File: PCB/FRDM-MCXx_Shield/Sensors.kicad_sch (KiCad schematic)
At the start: 9 parts, among them J7 Conn_01x06_Socket, U2 FXLS8974CF

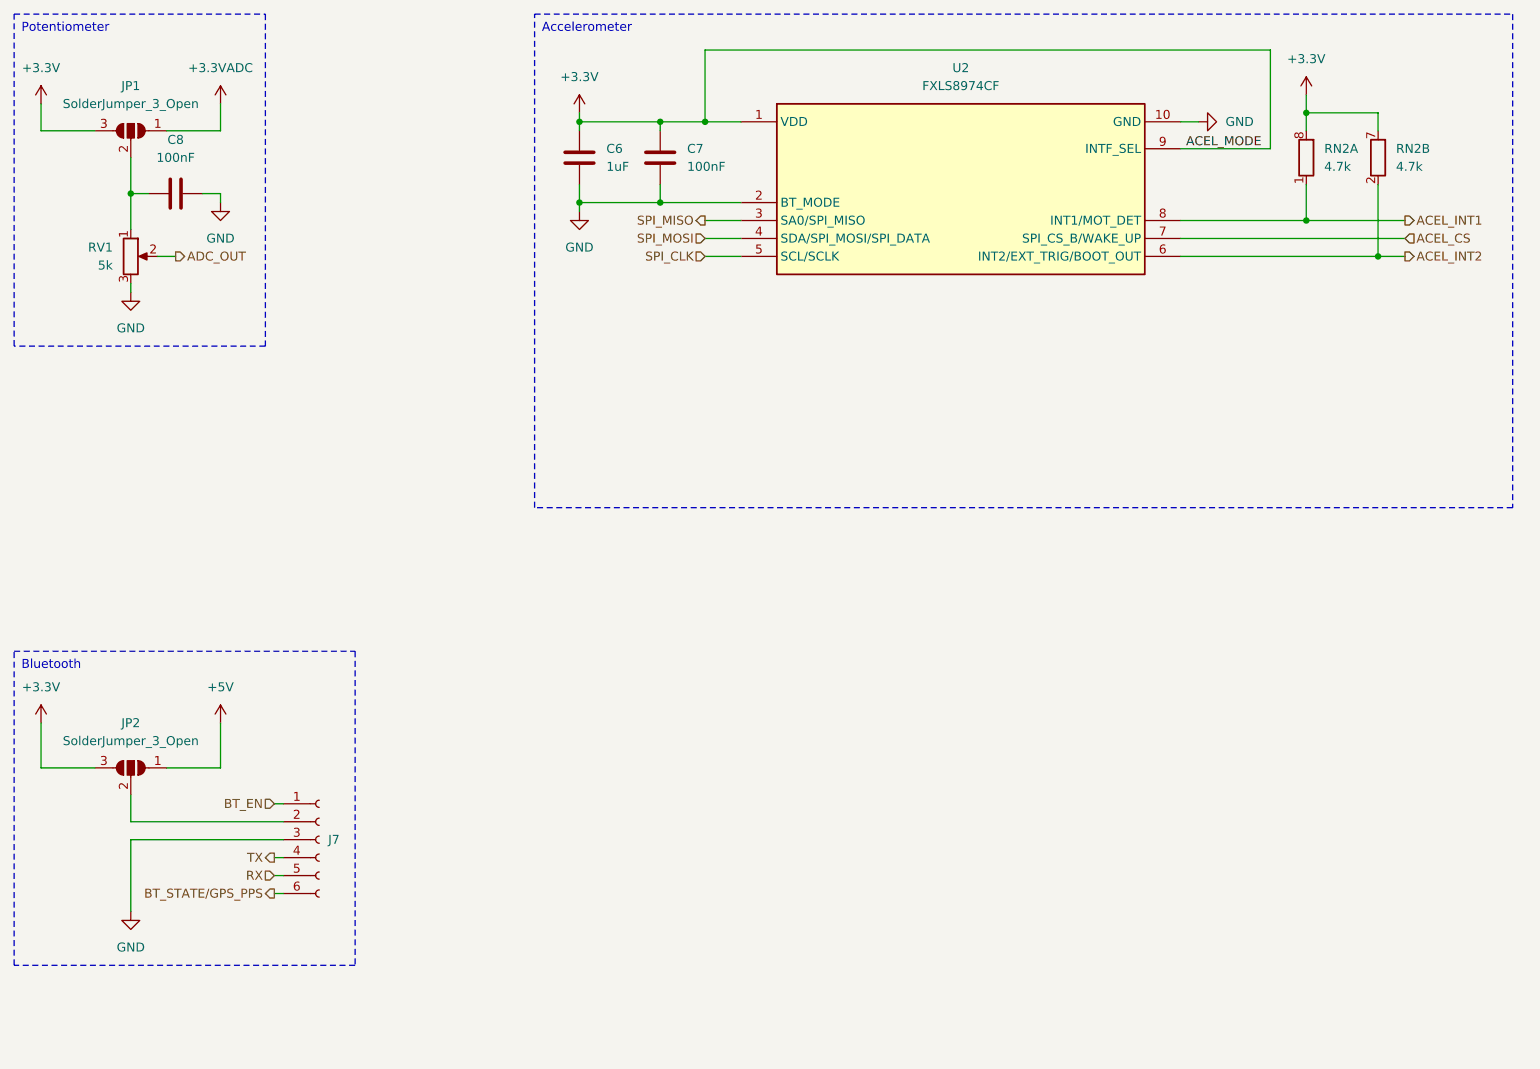
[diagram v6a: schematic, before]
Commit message: Update
Schematic: Fixed pinout, removed 5-9vin and a bunch of other stuff. Changed button/encoder debouncing.

PCB: Fixed pinout, layout and labeling. Added extra resisitors and capacitors.
Added diode direction markers.
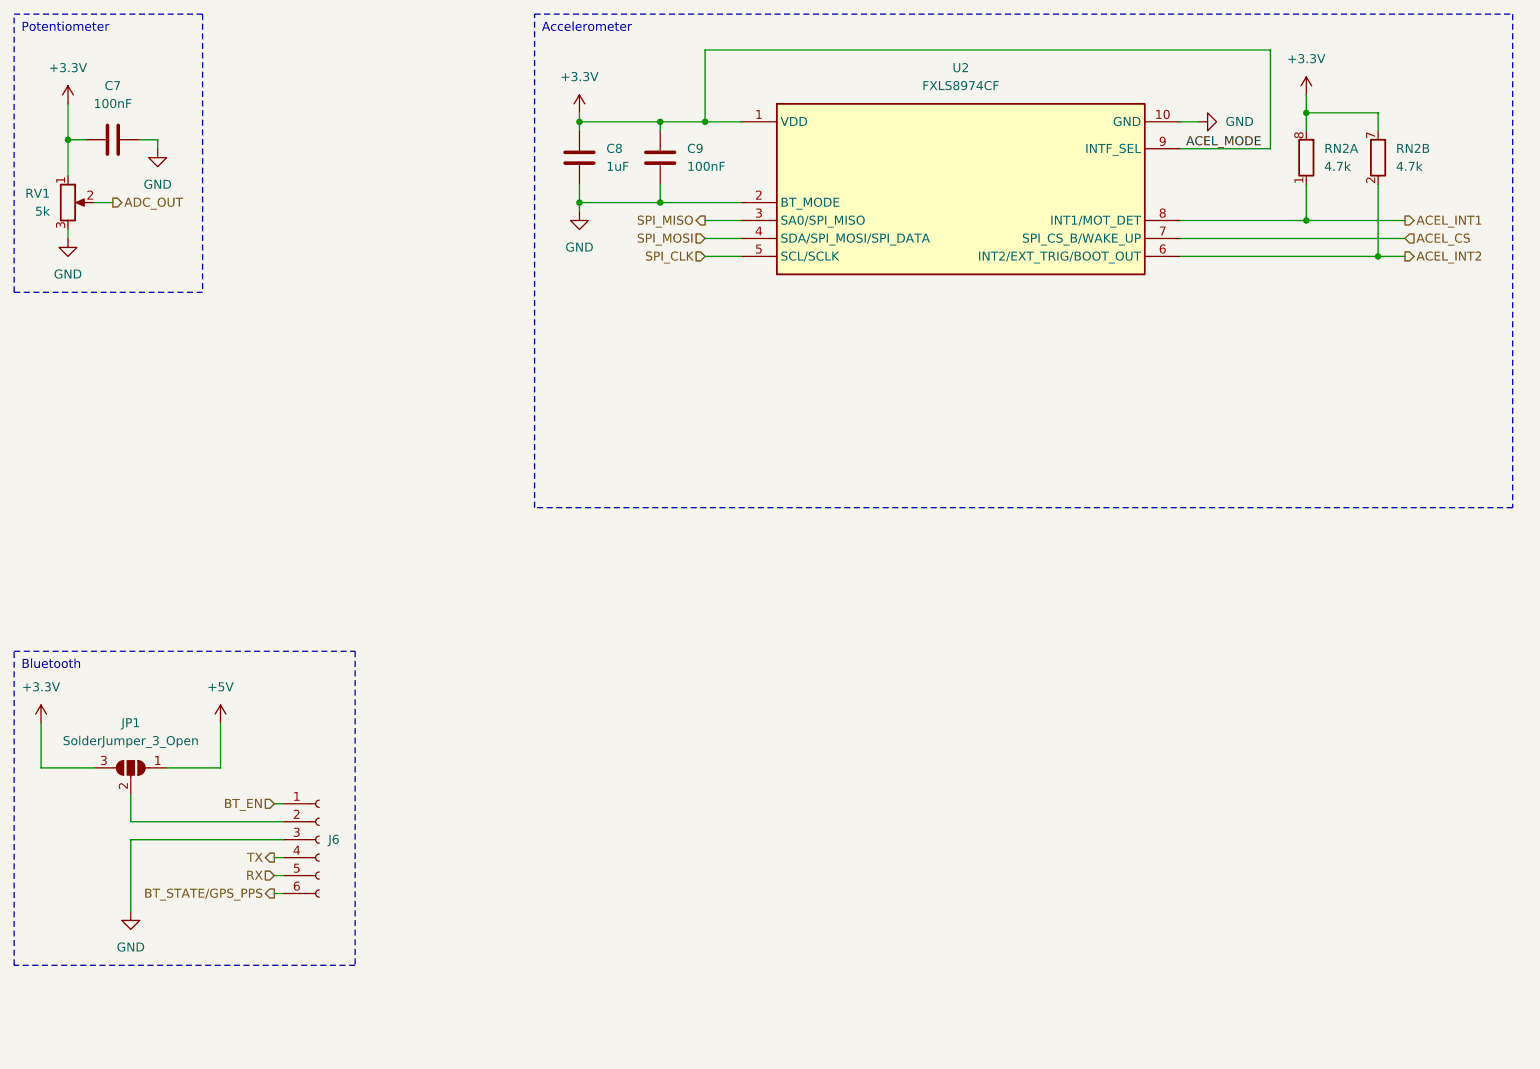
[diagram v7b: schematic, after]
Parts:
- removed JP1: SolderJumper_3_Open, Connector_PinHeader_2.54mm:PinHeader_1x03_P2.54mm_Vertical, symbol Jumper:SolderJumper_3_Open
- renumbered C8 to C7, C6 to C8, C7 to C9, J7 to J6, JP2 to JP1
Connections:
- net +3.3V: now also C7.1, RV1.1
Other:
- moved on the sheet: C7, RV1

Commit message: Updated footprint, PCB and schematic
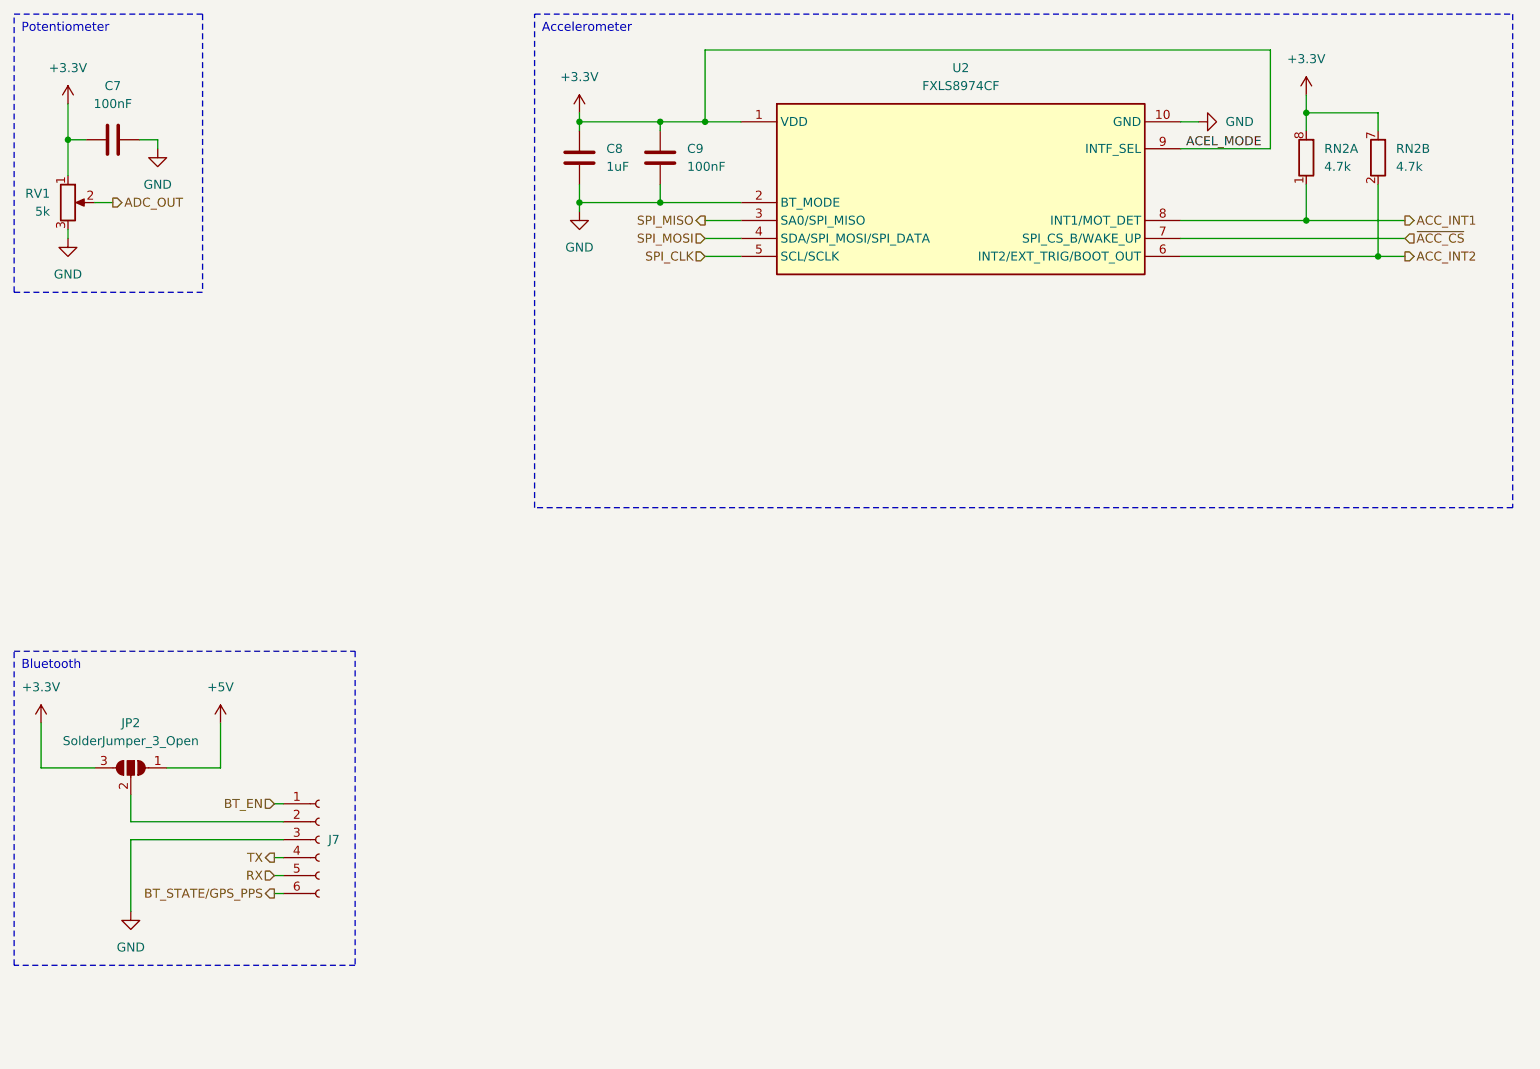
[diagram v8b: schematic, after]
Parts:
- renumbered J6 to J7, JP1 to JP2
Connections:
- net ACEL_CS renamed ~{ACC_CS}
- net ACEL_INT1 renamed ACC_INT1
- net ACEL_INT2 renamed ACC_INT2
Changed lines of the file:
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@@
   (title_block
     (title "Sensors")
-    (date "2024-02-22")
-    (rev "V1.1")
+    (date "2024-02-24")
+    (rev "V1.2")
     (company "HAN")
     (comment 1 "Authors: Thomas Ijseldijk, Hugo Arends & Emiel Visser")
@@
     (effects (font (size 1.27 1.27)) (justify left))
   )
-  (hierarchical_label "ACEL_CS" (shape input) (at 229.87 68.58 0) (fields_autoplaced)
+  (hierarchical_label "~{ACC_CS}" (shape input) (at 229.87 68.58 0) (fields_autoplaced)
     (effects (font (size 1.27 1.27)) (justify left))
   )
@@
     (effects (font (size 1.27 1.27)) (justify right))
   )
-  (hierarchical_label "ACEL_INT2" (shape output) (at 229.87 71.12 0) (fields_autoplaced)
+  (hierarchical_label "ACC_INT2" (shape output) (at 229.87 71.12 0) (fields_autoplaced)
     (effects (font (size 1.27 1.27)) (justify left))
   )
@@
     (effects (font (size 1.27 1.27)) (justify right))
   )
-  (hierarchical_label "ACEL_INT1" (shape output) (at 229.87 66.04 0) (fields_autoplaced)
+  (hierarchical_label "ACC_INT1" (shape output) (at 229.87 66.04 0) (fields_autoplaced)
     (effects (font (size 1.27 1.27)) (justify left))
   )
@@
   (symbol (lib_id "power:GND") (at 53.34 55.88 0) (unit 1)
     (in_bom yes) (on_board yes) (dnp no) (fields_autoplaced)
-    (property "Reference" "#PWR036" (at 53.34 62.23 0)
+    (property "Reference" "#PWR042" (at 53.34 62.23 0)
       (effects (font (size 1.27 1.27)) hide)
     )
@@
       (project "FRDM-MCXx_Shield"
         (path "/bffc27af-f9e0-4cc8-b5dc-88d2faf26a17/1dfdf8f6-c624-48d2-b647-f547c6376b37"
-          (reference "#PWR036") (unit 1)
+          (reference "#PWR042") (unit 1)
         )
       )
@@
   (symbol (lib_id "power:GND") (at 200.66 52.07 90) (unit 1)
     (in_bom yes) (on_board yes) (dnp no) (fields_autoplaced)
-    (property "Reference" "#PWR035" (at 207.01 52.07 0)
+    (property "Reference" "#PWR041" (at 207.01 52.07 0)
       (effects (font (size 1.27 1.27)) hide)
     )
@@
       (project "FRDM-MCXx_Shield"
         (path "/bffc27af-f9e0-4cc8-b5dc-88d2faf26a17/1dfdf8f6-c624-48d2-b647-f547c6376b37"
-          (reference "#PWR035") (unit 1)
+          (reference "#PWR041") (unit 1)
         )
       )
@@
   (symbol (lib_id "power:+3.3V") (at 40.64 49.53 0) (unit 1)
     (in_bom yes) (on_board yes) (dnp no) (fields_autoplaced)
-    (property "Reference" "#PWR033" (at 40.64 53.34 0)
+    (property "Reference" "#PWR039" (at 40.64 53.34 0)
       (effects (font (size 1.27 1.27)) hide)
     )
@@
       (project "FRDM-MCXx_Shield"
         (path "/bffc27af-f9e0-4cc8-b5dc-88d2faf26a17/1dfdf8f6-c624-48d2-b647-f547c6376b37"
-          (reference "#PWR033") (unit 1)
+          (reference "#PWR039") (unit 1)
         )
       )
@@
   (symbol (lib_id "power:+5V") (at 62.23 137.16 0) (unit 1)
     (in_bom yes) (on_board yes) (dnp no) (fields_autoplaced)
-    (property "Reference" "#PWR040" (at 62.23 140.97 0)
+    (property "Reference" "#PWR046" (at 62.23 140.97 0)
       (effects (font (size 1.27 1.27)) hide)
     )
@@
       (project "FRDM-MCXx_Shield"
         (path "/bffc27af-f9e0-4cc8-b5dc-88d2faf26a17/1dfdf8f6-c624-48d2-b647-f547c6376b37"
-          (reference "#PWR040") (unit 1)
+          (reference "#PWR046") (unit 1)
         )
       )
@@
   (symbol (lib_id "power:GND") (at 40.64 68.58 0) (unit 1)
     (in_bom yes) (on_board yes) (dnp no) (fields_autoplaced)
-    (property "Reference" "#PWR038" (at 40.64 74.93 0)
+    (property "Reference" "#PWR044" (at 40.64 74.93 0)
       (effects (font (size 1.27 1.27)) hide)
     )
@@
       (project "FRDM-MCXx_Shield"
         (path "/bffc27af-f9e0-4cc8-b5dc-88d2faf26a17/1dfdf8f6-c624-48d2-b647-f547c6376b37"
-          (reference "#PWR038") (unit 1)
+          (reference "#PWR044") (unit 1)
         )
       )
@@
         )
         (path "/bffc27af-f9e0-4cc8-b5dc-88d2faf26a17/1dfdf8f6-c624-48d2-b647-f547c6376b37"
-          (reference "#PWR032") (unit 1)
+          (reference "#PWR038") (unit 1)
         )
       )
@@
   (symbol (lib_id "power:GND") (at 113.03 64.77 0) (unit 1)
     (in_bom yes) (on_board yes) (dnp no) (fields_autoplaced)
-    (property "Reference" "#PWR037" (at 113.03 71.12 0)
+    (property "Reference" "#PWR043" (at 113.03 71.12 0)
       (effects (font (size 1.27 1.27)) hide)
     )
@@
       (project "FRDM-MCXx_Shield"
         (path "/bffc27af-f9e0-4cc8-b5dc-88d2faf26a17/1dfdf8f6-c624-48d2-b647-f547c6376b37"
-          (reference "#PWR037") (unit 1)
+          (reference "#PWR043") (unit 1)
         )
       )
@@
   (symbol (lib_id "power:GND") (at 49.53 163.83 0) (unit 1)
     (in_bom yes) (on_board yes) (dnp no) (fields_autoplaced)
-    (property "Reference" "#PWR041" (at 49.53 170.18 0)
+    (property "Reference" "#PWR047" (at 49.53 170.18 0)
       (effects (font (size 1.27 1.27)) hide)
     )
@@
       (project "FRDM-MCXx_Shield"
         (path "/bffc27af-f9e0-4cc8-b5dc-88d2faf26a17/1dfdf8f6-c624-48d2-b647-f547c6376b37"
-          (reference "#PWR041") (unit 1)
+          (reference "#PWR047") (unit 1)
         )
       )
@@
   (symbol (lib_id "Connector:Conn_01x06_Socket") (at 76.2 153.67 0) (unit 1)
     (in_bom yes) (on_board yes) (dnp no) (fields_autoplaced)
-    (property "Reference" "J6" (at 77.47 153.67 0)
+    (property "Reference" "J7" (at 77.47 153.67 0)
       (effects (font (size 1.27 1.27)) (justify left))
     )
@@
       (project "FRDM-MCXx_Shield"
         (path "/bffc27af-f9e0-4cc8-b5dc-88d2faf26a17/1dfdf8f6-c624-48d2-b647-f547c6376b37"
-          (reference "J6") (unit 1)
+          (reference "J7") (unit 1)
         )
       )
@@
   (symbol (lib_id "power:+3.3V") (at 36.83 137.16 0) (unit 1)
     (in_bom yes) (on_board yes) (dnp no) (fields_autoplaced)
-    (property "Reference" "#PWR039" (at 36.83 140.97 0)
+    (property "Reference" "#PWR045" (at 36.83 140.97 0)
       (effects (font (size 1.27 1.27)) hide)
     )
@@
       (project "FRDM-MCXx_Shield"
         (path "/bffc27af-f9e0-4cc8-b5dc-88d2faf26a17/1dfdf8f6-c624-48d2-b647-f547c6376b37"
-          (reference "#PWR039") (unit 1)
+          (reference "#PWR045") (unit 1)
         )
       )
@@
   (symbol (lib_id "power:+3.3V") (at 113.03 50.8 0) (unit 1)
     (in_bom yes) (on_board yes) (dnp no) (fields_autoplaced)
-    (property "Reference" "#PWR034" (at 113.03 54.61 0)
+    (property "Reference" "#PWR040" (at 113.03 54.61 0)
       (effects (font (size 1.27 1.27)) hide)
     )
@@
       (project "FRDM-MCXx_Shield"
         (path "/bffc27af-f9e0-4cc8-b5dc-88d2faf26a17/1dfdf8f6-c624-48d2-b647-f547c6376b37"
-          (reference "#PWR034") (unit 1)
+          (reference "#PWR040") (unit 1)
         )
       )
@@
   (symbol (lib_id "Jumper:SolderJumper_3_Open") (at 49.53 143.51 0) (mirror y) (unit 1)
     (in_bom yes) (on_board yes) (dnp no)
-    (property "Reference" "JP1" (at 49.53 137.16 0)
+    (property "Reference" "JP2" (at 49.53 137.16 0)
       (effects (font (size 1.27 1.27)))
     )
@@
       (project "FRDM-MCXx_Shield"
         (path "/bffc27af-f9e0-4cc8-b5dc-88d2faf26a17/1dfdf8f6-c624-48d2-b647-f547c6376b37"
-          (reference "JP1") (unit 1)
-        )
-      )
+          (reference "JP2") (unit 1)
+        )
+      )
